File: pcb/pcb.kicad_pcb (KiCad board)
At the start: 2 copper layers, 59 x 66 mm, 5 parts, among them J1 LM2596 OUTPUT, J2 PCA9685, J3 20A 300W High-Power Buck Conv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, J4 ESP32_1, J5 ESP32_2

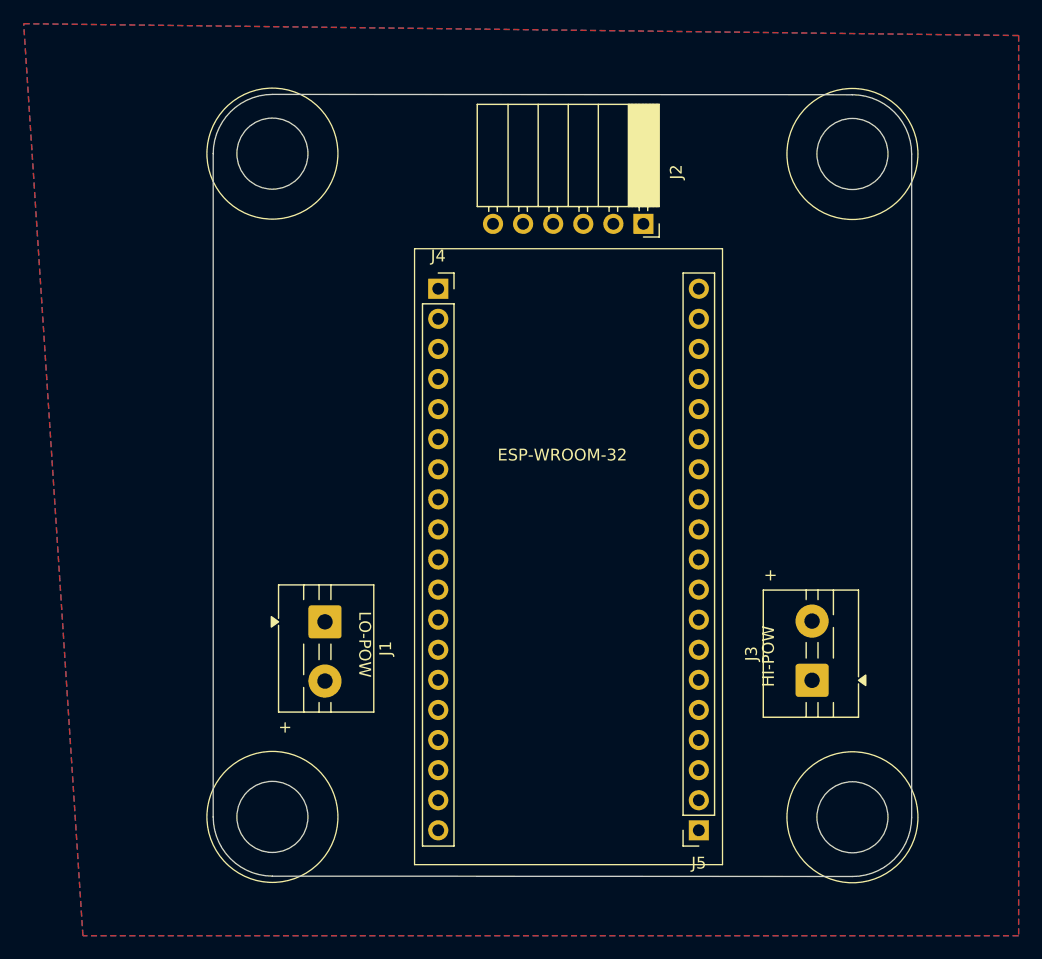
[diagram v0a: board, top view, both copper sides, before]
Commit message: Modify power management on PCB. Battery, high power buck converter I/O & low power buck converter input remain off board. Reduce screw hole size.
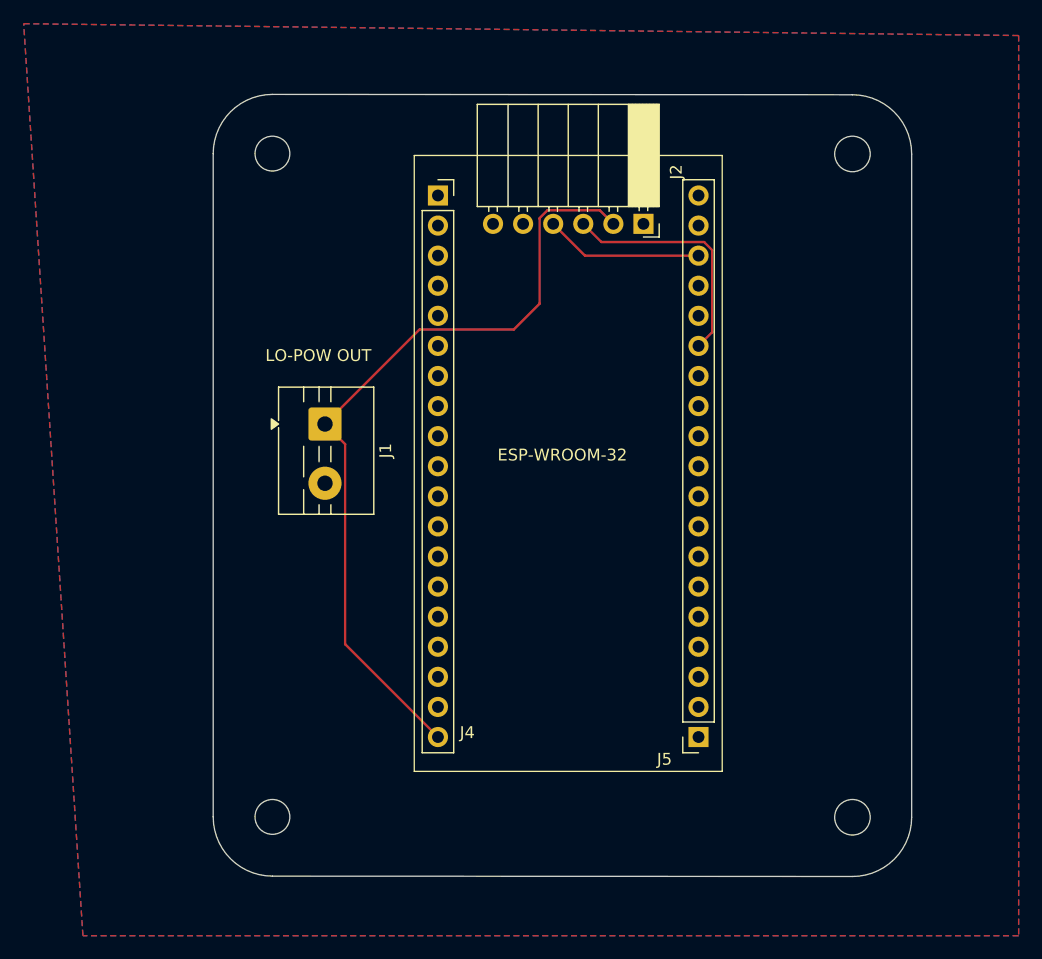
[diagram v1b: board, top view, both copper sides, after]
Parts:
- removed J3: 20A 300W High-Power Buck Converter OUTPUT, TerminalBlock:TerminalBlock_MaiXu_MX126-5.0-02P_1x02_P5.00mm
- moved J1 16.7 mm to (102.4, 77.8)
- moved J5 7.88 mm to (134.0, 104.2)
- moved J4 7.88 mm to (112.0, 58.5)
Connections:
- J1 pad 1: GND -> +5V
- J1 pad 2: +5V -> GND
- J2 pad 1: +6.8V -> unconnected-(J2-Pin_1-Pad1)
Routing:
- net +5V: track 0.00 -> 66.9 mm
- net Net-(J2-Pin_3): track 0.00 -> 20.4 mm
- net Net-(J2-Pin_4): track 0.00 -> 13.4 mm
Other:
- outline, holes or cut-outs redrawn
- board text added: "LO-POW OUT"
- board text removed: "+"
- board text removed: "HI-POW"
- board text removed: "LO-POW"

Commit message: Fix: Add dedicated 6.8V copper fill to PCB where a 1x12 header pin is used to power servos. Fixes bottleneck of using the PCA9685 chip to power the servos (doesn't allow for 20A stall current due to simple PCB traces.)
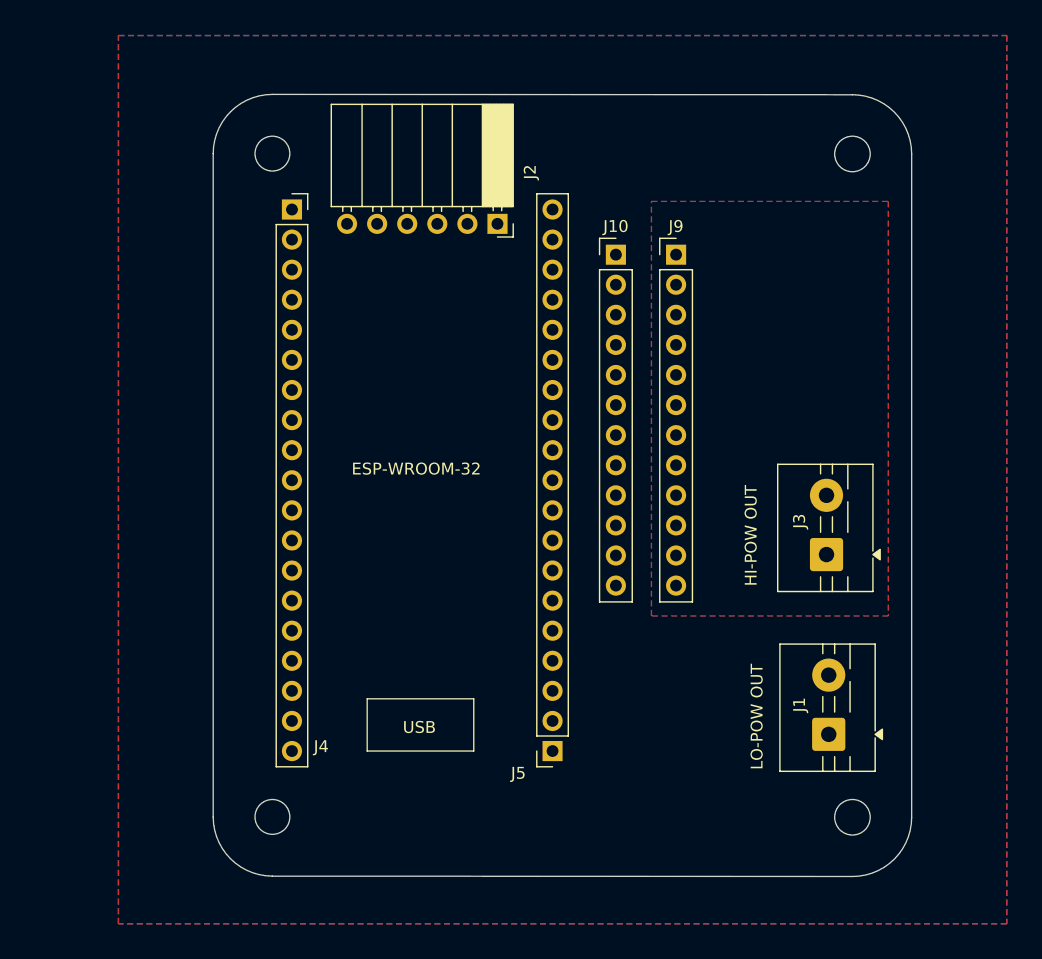
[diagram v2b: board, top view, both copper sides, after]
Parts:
- added J10: Servo -, Connector_PinHeader_2.54mm:PinHeader_1x12_P2.54mm_Vertical, F.Cu at (127.0, 63.5)
- added J3: 20A 300W High-Power Buck Converter OUTPUT, TerminalBlock:TerminalBlock_MaiXu_MX126-5.0-02P_1x02_P5.00mm, F.Cu at (144.8, 88.8)
- added J9: Servo +, Connector_PinHeader_2.54mm:PinHeader_1x12_P2.54mm_Vertical, F.Cu at (132.1, 63.5)
- moved J1 50.0 mm to (145.0, 104.0), turned to 90 degrees
- moved J4 12.4 mm to (99.7, 59.7)
- moved J5 12.4 mm to (121.7, 105.4)
- moved J2 12.3 mm to (117.0, 60.9)
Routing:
- net +5V: track 66.9 -> 0.00 mm
- net Net-(J2-Pin_3): track 20.4 -> 0.00 mm
- net Net-(J2-Pin_4): track 13.4 -> 0.00 mm
- added copper zone on F.Cu, net +6.8V
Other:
- board text added: "HI-POW OUT"
- board text added: "USB"

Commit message: Fix: short caused by screw terminal's GND being in 6.8V copper fill. Rearrange components to better integrate in CAD.
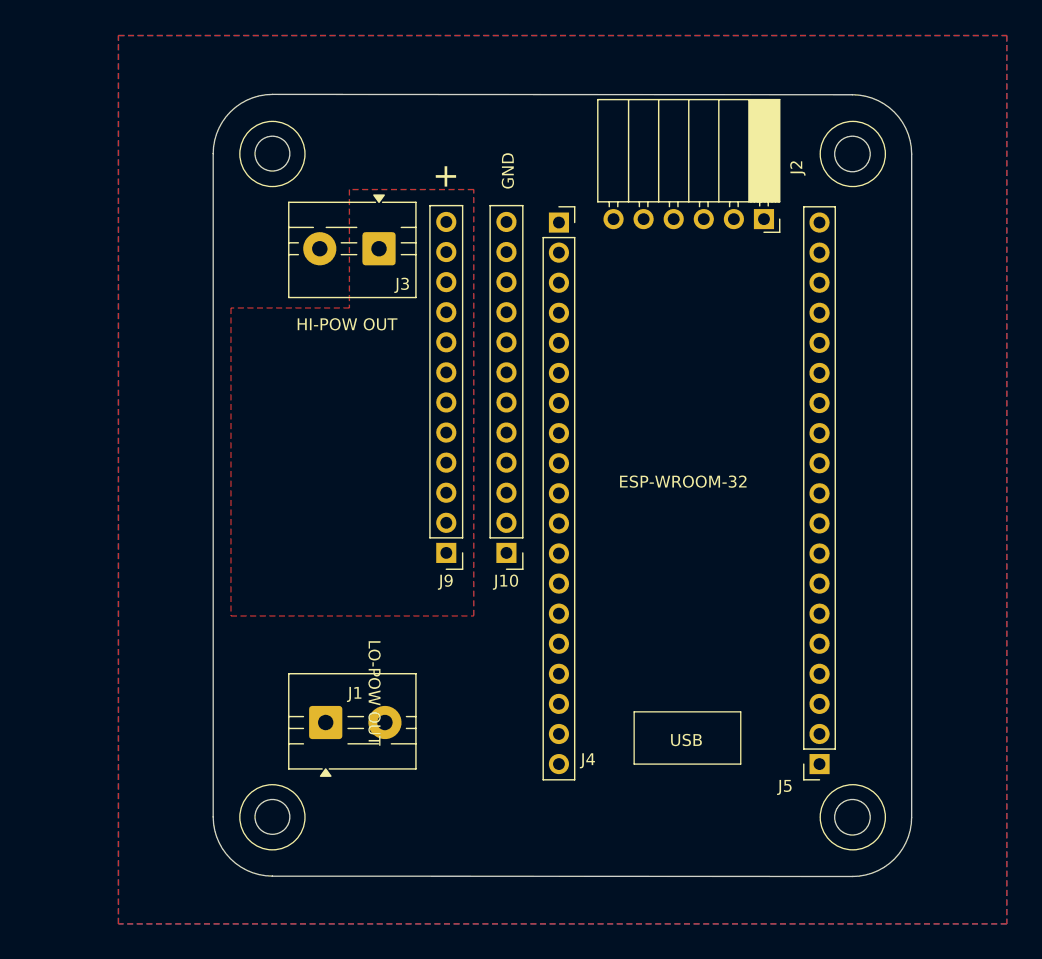
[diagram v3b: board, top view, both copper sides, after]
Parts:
- moved J3 45.8 mm to (107.0, 63.0), turned to 180 degrees
- moved J1 42.5 mm to (102.5, 103.0), turned to 0 degrees
- moved J9 31.8 mm to (112.7, 88.7), turned to 180 degrees
- moved J10 26.8 mm to (117.8, 88.7), turned to 180 degrees
- moved J4 22.6 mm to (122.2, 60.8)
- moved J5 22.6 mm to (144.2, 106.5)
- moved J2 22.5 mm to (139.5, 60.5)
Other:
- board text added: "+"
- board text added: "GND"
